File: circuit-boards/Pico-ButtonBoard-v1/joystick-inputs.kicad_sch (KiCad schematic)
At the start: 25 parts, among them J25 XY0-R, J26 XY1-L, U7 MCP3201T-CI/SN, U9 MCP1700T-3302E/TT

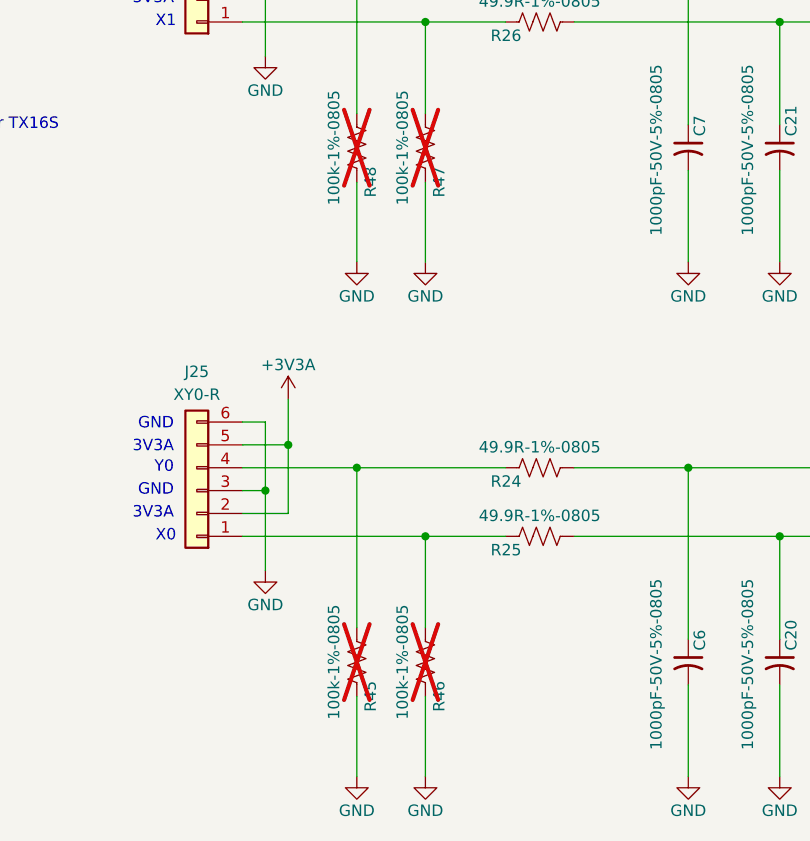
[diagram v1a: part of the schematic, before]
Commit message: Lower impedance of battery override input
Signed-off-by: Scott Berman <scott.berman@bluerivertech.com>
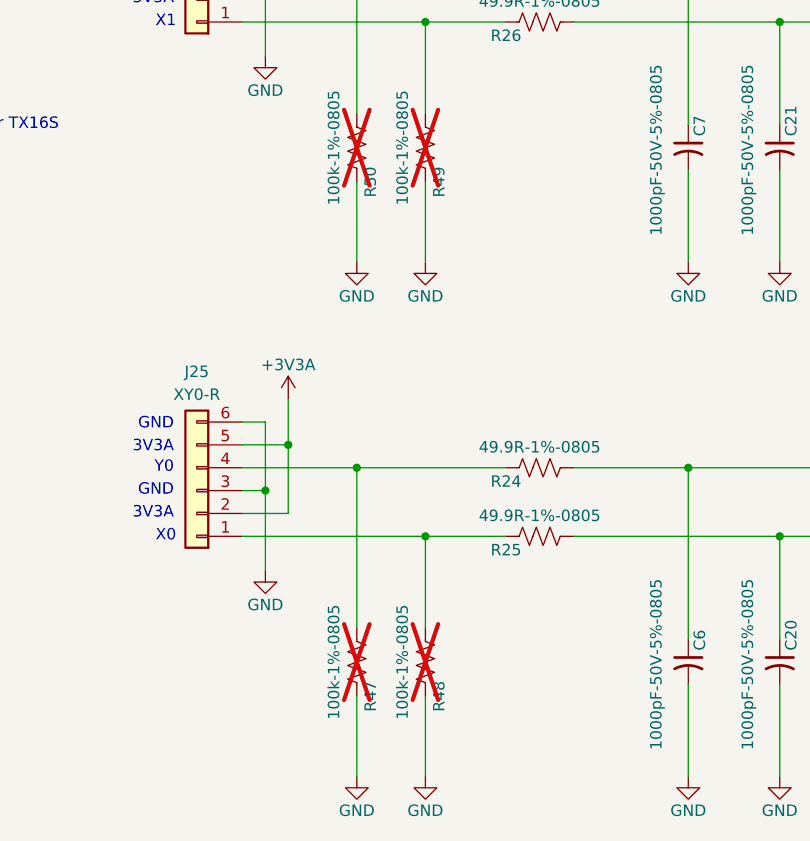
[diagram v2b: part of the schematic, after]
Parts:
- renumbered R45 to R47, R46 to R48, R47 to R49, R48 to R50
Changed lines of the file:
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@@
 	(title_block
 		(title "Pico Button Board")
-		(date "2026-01-20")
+		(date "2026-01-21")
 		(rev "1")
 	)
@@
 			)
 		)
+		(property "Sim.Pins" ""
+			(at 276.86 78.74 0)
+			(effects
+				(font
+					(size 1.27 1.27)
+				)
+				(hide yes)
+			)
+		)
 		(pin "2"
 		)
@@
 			)
 		)
+		(property "Sim.Pins" ""
+			(at 284.48 71.12 0)
+			(effects
+				(font
+					(size 1.27 1.27)
+				)
+				(hide yes)
+			)
+		)
 		(pin "1"
 		)
@@
 			)
 		)
+		(property "Sim.Pins" ""
+			(at 110.49 205.74 0)
+			(effects
+				(font
+					(size 1.27 1.27)
+				)
+				(hide yes)
+			)
+		)
 		(pin "3"
 		)
@@
 			)
 		)
+		(property "Sim.Pins" ""
+			(at 148.59 210.82 90)
+			(effects
+				(font
+					(size 1.27 1.27)
+				)
+				(hide yes)
+			)
+		)
 		(pin "1"
 		)
@@
 		(on_board yes)
 		(dnp yes)
-		(property "Reference" "R48"
+		(property "Reference" "R50"
 			(at 129.794 171.45 90)
 			(effects
@@
 			)
 		)
+		(property "Sim.Pins" ""
+			(at 128.27 167.64 90)
+			(effects
+				(font
+					(size 1.27 1.27)
+				)
+				(hide yes)
+			)
+		)
 		(pin "1"
 		)
@@
 			(project "Pico-ButtonBoard-v1"
 				(path "/644201a9-3a2f-4df3-9c93-2ae55394df4b/685073ee-f919-44b0-8568-43a13e57da9c"
-					(reference "R48")
+					(reference "R50")
 					(unit 1)
 				)
@@
 			)
 		)
+		(property "Sim.Pins" ""
+			(at 165.1 224.79 90)
+			(effects
+				(font
+					(size 1.27 1.27)
+				)
+				(hide yes)
+			)
+		)
 		(pin "2"
 		)
@@
 			)
 		)
+		(property "Sim.Pins" ""
+			(at 165.1 167.64 90)
+			(effects
+				(font
+					(size 1.27 1.27)
+				)
+				(hide yes)
+			)
+		)
 		(pin "2"
 		)
@@
 			)
 		)
+		(property "Sim.Pins" ""
+			(at 148.59 146.05 90)
+			(effects
+				(font
+					(size 1.27 1.27)
+				)
+				(hide yes)
+			)
+		)
 		(pin "1"
 		)
@@
 			)
 		)
+		(property "Sim.Pins" ""
+			(at 148.59 153.67 90)
+			(effects
+				(font
+					(size 1.27 1.27)
+				)
+				(hide yes)
+			)
+		)
 		(pin "1"
 		)
@@
 			)
 		)
+		(property "Sim.Pins" ""
+			(at 231.14 137.16 0)
+			(effects
+				(font
+					(size 1.27 1.27)
+				)
+				(hide yes)
+			)
+		)
 		(pin "4"
 		)
@@
 			)
 		)
+		(property "Sim.Pins" ""
+			(at 149.86 71.12 90)
+			(effects
+				(font
+					(size 1.27 1.27)
+				)
+				(hide yes)
+			)
+		)
 		(pin "1"
 		)
@@
 			)
 		)
+		(property "Sim.Pins" ""
+			(at 223.52 119.38 0)
+			(effects
+				(font
+					(size 1.27 1.27)
+				)
+				(hide yes)
+			)
+		)
 		(pin "2"
 		)
@@
 			)
 		)
+		(property "Sim.Pins" ""
+			(at 196.85 78.74 0)
+			(effects
+				(font
+					(size 1.27 1.27)
+				)
+				(hide yes)
+			)
+		)
 		(pin "2"
 		)
@@
 		(on_board yes)
 		(dnp yes)
-		(property "Reference" "R46"
+		(property "Reference" "R48"
 			(at 137.414 228.6 90)
 			(effects
@@
 			)
 		)
+		(property "Sim.Pins" ""
+			(at 135.89 224.79 90)
+			(effects
+				(font
+					(size 1.27 1.27)
+				)
+				(hide yes)
+			)
+		)
 		(pin "1"
 		)
@@
 			(project "Pico-ButtonBoard-v1"
 				(path "/644201a9-3a2f-4df3-9c93-2ae55394df4b/685073ee-f919-44b0-8568-43a13e57da9c"
-					(reference "R46")
+					(reference "R48")
 					(unit 1)
 				)
@@
 			)
 		)
+		(property "Sim.Pins" ""
+			(at 129.54 78.74 0)
+			(effects
+				(font
+					(size 1.27 1.27)
+				)
+				(hide yes)
+			)
+		)
 		(pin "2"
 		)
@@
 			)
 		)
+		(property "Sim.Pins" ""
+			(at 284.48 100.33 0)
+			(effects
+				(font
+					(size 1.27 1.27)
+				)
+				(hide yes)
+			)
+		)
 		(pin "1"
 		)
@@
 			)
 		)
+		(property "Sim.Pins" ""
+			(at 175.26 224.79 90)
+			(effects
+				(font
+					(size 1.27 1.27)
+				)
+				(hide yes)
+			)
+		)
 		(pin "2"
 		)
@@
 			)
 		)
+		(property "Sim.Pins" ""
+			(at 233.68 71.12 0)
+			(effects
+				(font
+					(size 1.27 1.27)
+				)
+				(hide yes)
+			)
+		)
 		(pin "2"
 		)
@@
 			)
 		)
+		(property "Sim.Pins" ""
+			(at 148.59 203.2 90)
+			(effects
+				(font
+					(size 1.27 1.27)
+				)
+				(hide yes)
+			)
+		)
 		(pin "1"
 		)
@@
 			)
 		)
+		(property "Sim.Pins" ""
+			(at 189.23 78.74 0)
+			(effects
+				(font
+					(size 1.27 1.27)
+				)
+				(hide yes)
+			)
+		)
 		(pin "2"
 		)
@@
 			)
 		)
+		(property "Sim.Pins" ""
+			(at 269.24 78.74 0)
+			(effects
+				(font
+					(size 1.27 1.27)
+				)
+				(hide yes)
+			)
+		)
 		(pin "2"
 		)
@@
 			)
 		)
+		(property "Sim.Pins" ""
+			(at 110.49 148.59 0)
+			(effects
+				(font
+					(size 1.27 1.27)
+				)
+				(hide yes)
+			)
+		)
 		(pin "3"
 		)
@@
 		(on_board yes)
 		(dnp yes)
-		(property "Reference" "R47"
+		(property "Reference" "R49"
 			(at 137.414 171.45 90)
 			(effects
@@
 			)
 		)
+		(property "Sim.Pins" ""
+			(at 135.89 167.64 90)
+			(effects
+				(font
+					(size 1.27 1.27)
+				)
+				(hide yes)
+			)
+		)
 		(pin "1"
 		)
@@
 			(project "Pico-ButtonBoard-v1"
 				(path "/644201a9-3a2f-4df3-9c93-2ae55394df4b/685073ee-f919-44b0-8568-43a13e57da9c"
-					(reference "R47")
+					(reference "R49")
 					(unit 1)
 				)
@@
 			)
 		)
+		(property "Sim.Pins" ""
+			(at 175.26 167.64 90)
+			(effects
+				(font
+					(size 1.27 1.27)
+				)
+				(hide yes)
+			)
+		)
 		(pin "2"
 		)
@@
 		(on_board yes)
 		(dnp yes)
-		(property "Reference" "R45"
+		(property "Reference" "R47"
 			(at 129.794 228.6 90)
 			(effects
@@
 			)
 		)
+		(property "Sim.Pins" ""
+			(at 128.27 224.79 90)
+			(effects
+				(font
+					(size 1.27 1.27)
+				)
+				(hide yes)
+			)
+		)
 		(pin "1"
 		)
@@
 			(project "Pico-ButtonBoard-v1"
 				(path "/644201a9-3a2f-4df3-9c93-2ae55394df4b/685073ee-f919-44b0-8568-43a13e57da9c"
-					(reference "R45")
+					(reference "R47")
 					(unit 1)
 				)
